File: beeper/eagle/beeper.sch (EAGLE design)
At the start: 30 parts, among them J4 ICSP, T1 MMBT3904, U1 ATA6631, U2 ATMEGA328P, X1 16MHz

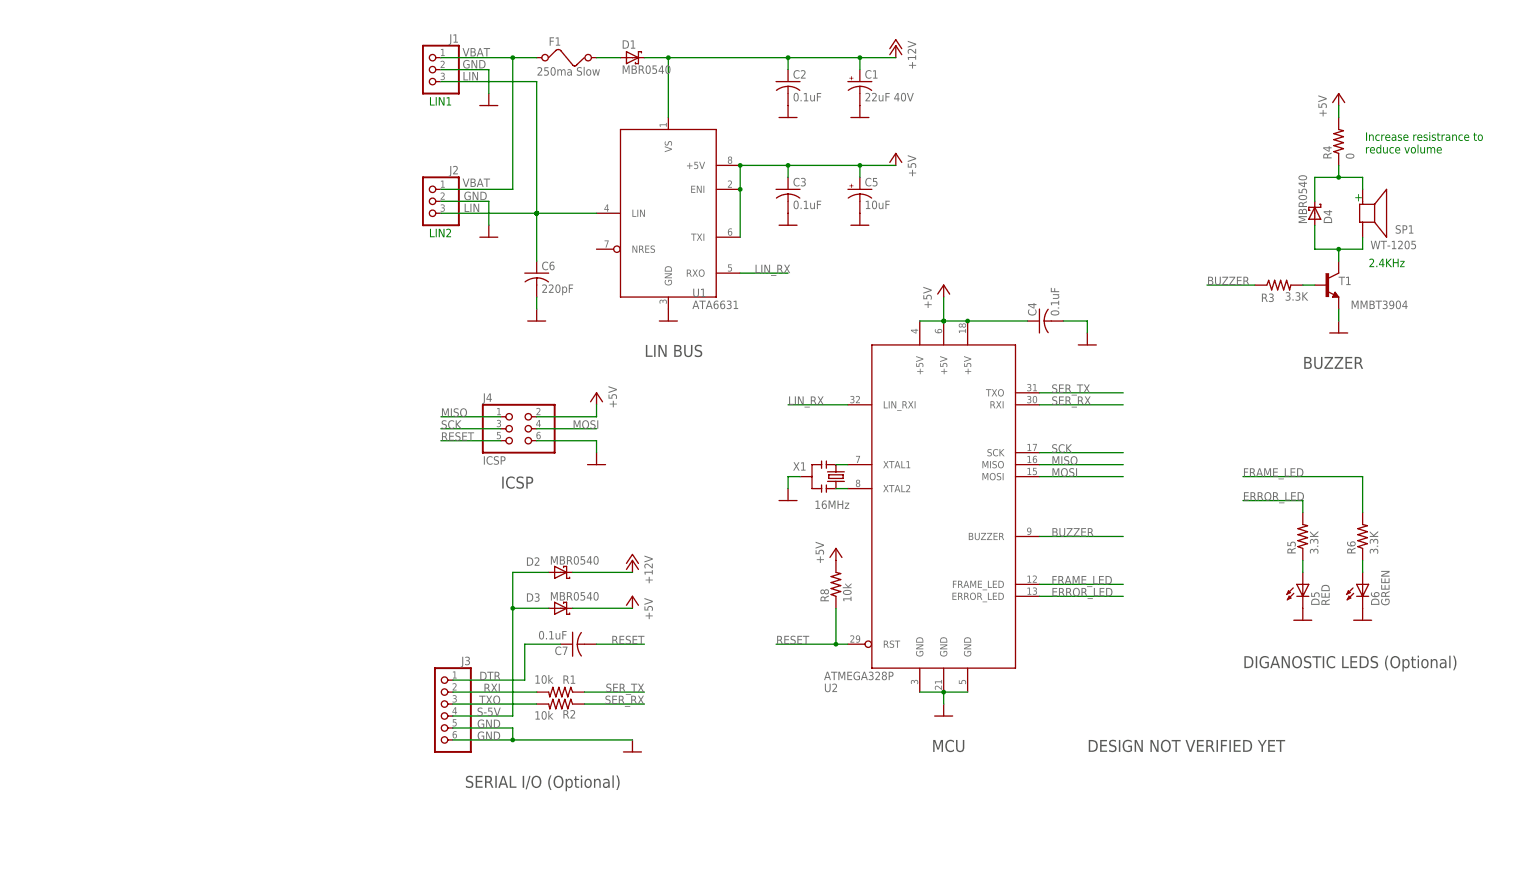
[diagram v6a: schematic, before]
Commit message: More beeper library cleanup.
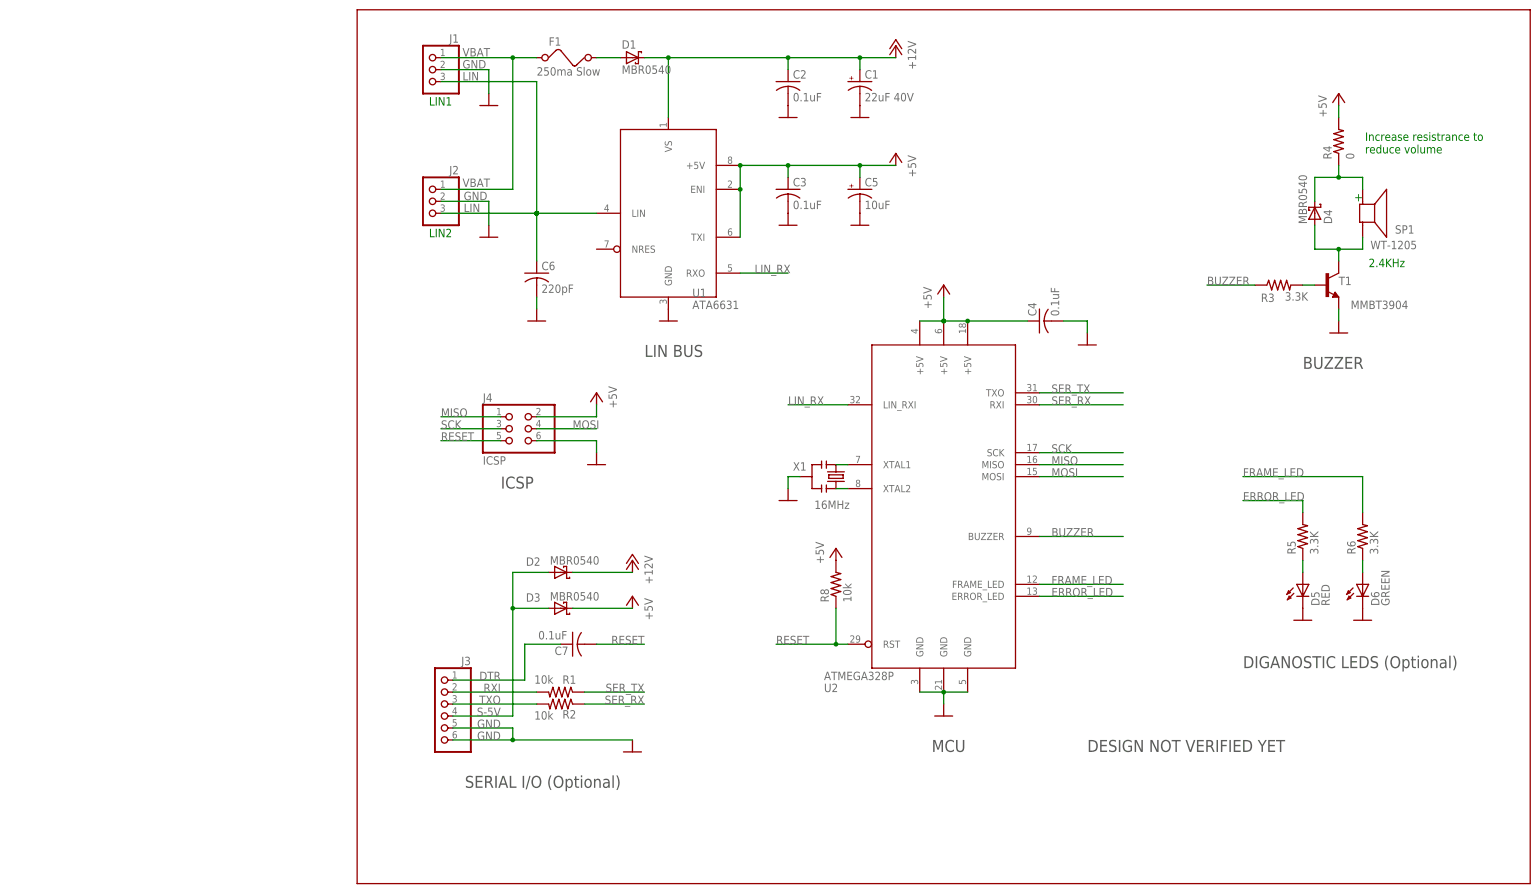
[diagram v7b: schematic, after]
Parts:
- C4: device rcl:C-USC0805 -> beeper:C-USC0805
- R3: device rcl:R-US_R0805 -> beeper:R-US_R0805
- T1: device transistor:MMBT3904LT1-NPN-SOT23-BEC -> beeper:MMBT3904LT1-NPN-SOT23-BEC
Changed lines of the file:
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@@
 <part name="C6" library="beeper" deviceset="C-US" device="C0805" value="220pF"/>
 <part name="J1" library="beeper" deviceset="PINHD-1X3" device=""/>
-<part name="FRAME2" library="frames" deviceset="LETTER_L" device=""/>
 <part name="GND3" library="beeper" deviceset="GND" device=""/>
 <part name="GND5" library="beeper" deviceset="GND" device=""/>
@@
 <part name="GND14" library="beeper" deviceset="GND" device=""/>
 <part name="P+5" library="beeper" deviceset="+5V" device=""/>
-<part name="R3" library="rcl" deviceset="R-US_" device="R0805" value="3.3K"/>
-<part name="T1" library="transistor" deviceset="*-NPN-" device="SOT23-BEC" technology="MMBT3904LT1" value="MMBT3904"/>
+<part name="R3" library="beeper" deviceset="R-US_" device="R0805" value="3.3K"/>
+<part name="T1" library="beeper" deviceset="*-NPN-" device="SOT23-BEC" technology="MMBT3904LT1" value="MMBT3904"/>
 <part name="GND18" library="beeper" deviceset="GND" device=""/>
 <part name="P+3" library="beeper" deviceset="+5V" device=""/>
@@
 <part name="C2" library="beeper" deviceset="C-US" device="C0805" value="0.1uF"/>
 <part name="C5" library="beeper" deviceset="CPOL-US" device="A/3216-18R" value="10uF"/>
-<part name="C4" library="rcl" deviceset="C-US" device="C0805" value="0.1uF"/>
+<part name="C4" library="beeper" deviceset="C-US" device="C0805" value="0.1uF"/>
 <part name="GND9" library="beeper" deviceset="GND" device=""/>
 <part name="GND10" library="beeper" deviceset="GND" device=""/>
@@
 <part name="P+8" library="beeper" deviceset="+5V" device=""/>
 <part name="P+9" library="beeper" deviceset="+12V" device=""/>
+<part name="U$1" library="beeper" deviceset="DOCFIELD" device=""/>
 </parts>
 <sheets>
@@
 <text x="274.828" y="180.34" size="1.778" layer="91">Increase resistrance to
 reduce volume</text>
+<wire x1="60.96" y1="210.82" x2="309.88" y2="210.82" width="0.1524" layer="94"/>
+<wire x1="309.88" y1="210.82" x2="309.88" y2="25.4" width="0.1524" layer="94"/>
+<wire x1="309.88" y1="25.4" x2="60.96" y2="25.4" width="0.1524" layer="94"/>
+<wire x1="60.96" y1="25.4" x2="60.96" y2="210.82" width="0.1524" layer="94"/>
 </plain>
 <instances>
@@
 <instance part="C6" gate="G$1" x="99.06" y="154.94"/>
 <instance part="J1" gate="A" x="76.2" y="198.12" rot="MR0"/>
-<instance part="FRAME2" gate="G$1" x="60.96" y="25.4"/>
-<instance part="FRAME2" gate="G$2" x="208.28" y="25.4"/>
 <instance part="GND3" gate="1" x="261.62" y="81.28"/>
 <instance part="GND5" gate="1" x="119.38" y="53.34" rot="MR0"/>
@@
 <instance part="P+8" gate="1" x="175.26" y="180.34" rot="MR0"/>
 <instance part="P+9" gate="1" x="175.26" y="203.2" rot="MR0"/>
+<instance part="U$1" gate="G$1" x="208.28" y="25.4"/>
 </instances>
 <busses>

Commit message: Updated beeper board and schematic for Rev B.
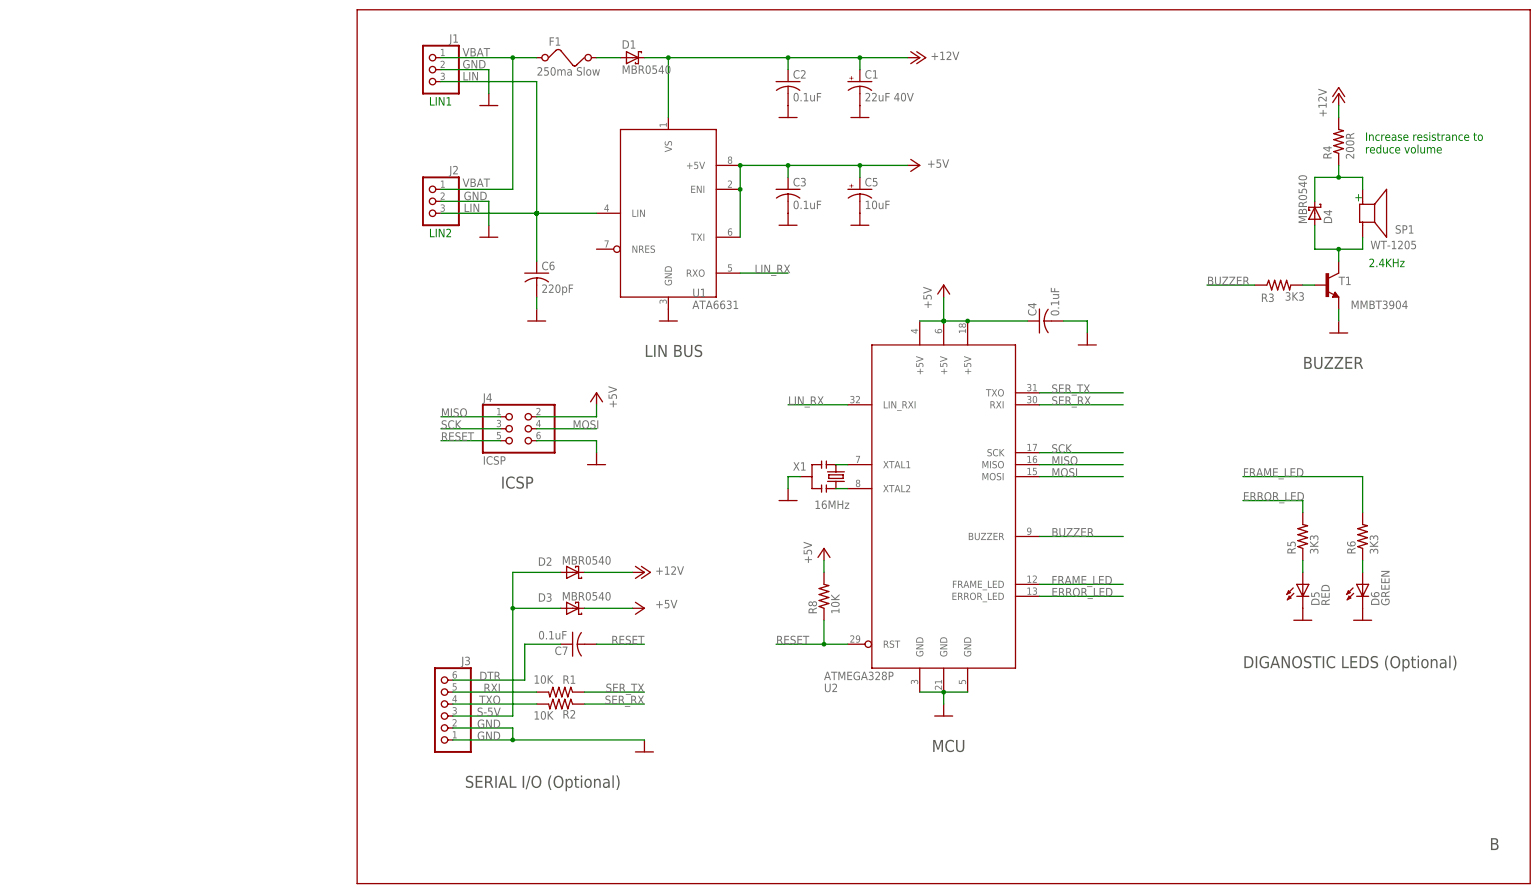
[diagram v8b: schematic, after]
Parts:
- D5, D6: device beeper:LEDSMT1206 -> beeper:LED
- R1, R2, R8: value 10k -> 10K
- R3, R5, R6: value 3.3K -> 3K3
- R4: value 0 -> 200R
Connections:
- net +12V: now also R4.2
- net +5V: no longer R4.2
- net DTR: now also J3.6; no longer J3.1
- net GND: now also J3.1, J3.2; no longer J3.5, J3.6
- net RXI: now also J3.5; no longer J3.2
- net S-5V: now also J3.3; no longer J3.4
- net TXO: now also J3.4; no longer J3.3
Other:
- note added: "B"
- note removed: "DESIGN NOT VERIFIED YET"
- moved on the sheet: D2, D3, R8
